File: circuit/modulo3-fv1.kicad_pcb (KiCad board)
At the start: 2 copper layers, 84 x 52 mm, 57 parts, among them J2 HOLE, J4 HOLE, J5 HOLE, J7 HOLE, U1 OPA1642, U10 TLE2426, U2 FV1_CONN, U3 FV-1, U4 PWR_CONN, U5 LM1117 3V3, U6 DIFFAUDIO, U7 AD5142A, U8 AMPCTRL, U9 PREAMP, Y1 32768Hz

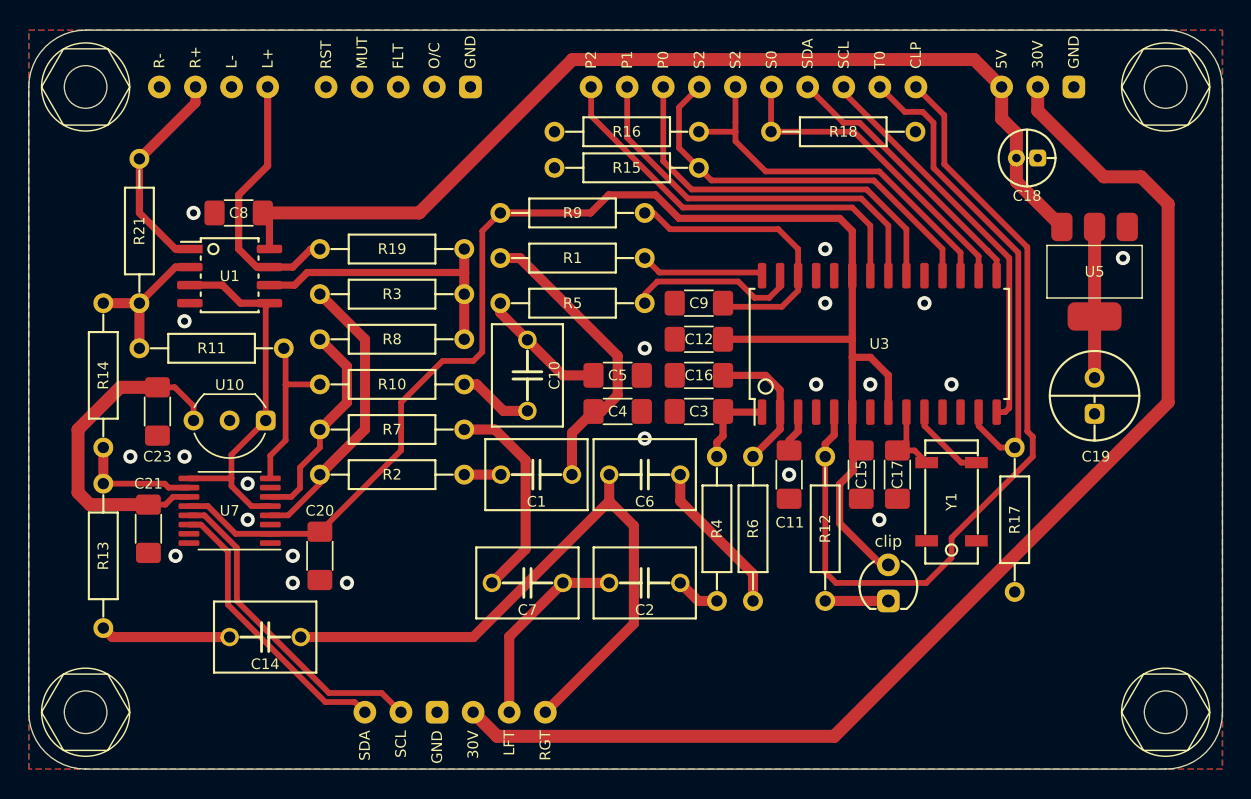
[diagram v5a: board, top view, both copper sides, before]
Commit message: tweaked power amp and fv1
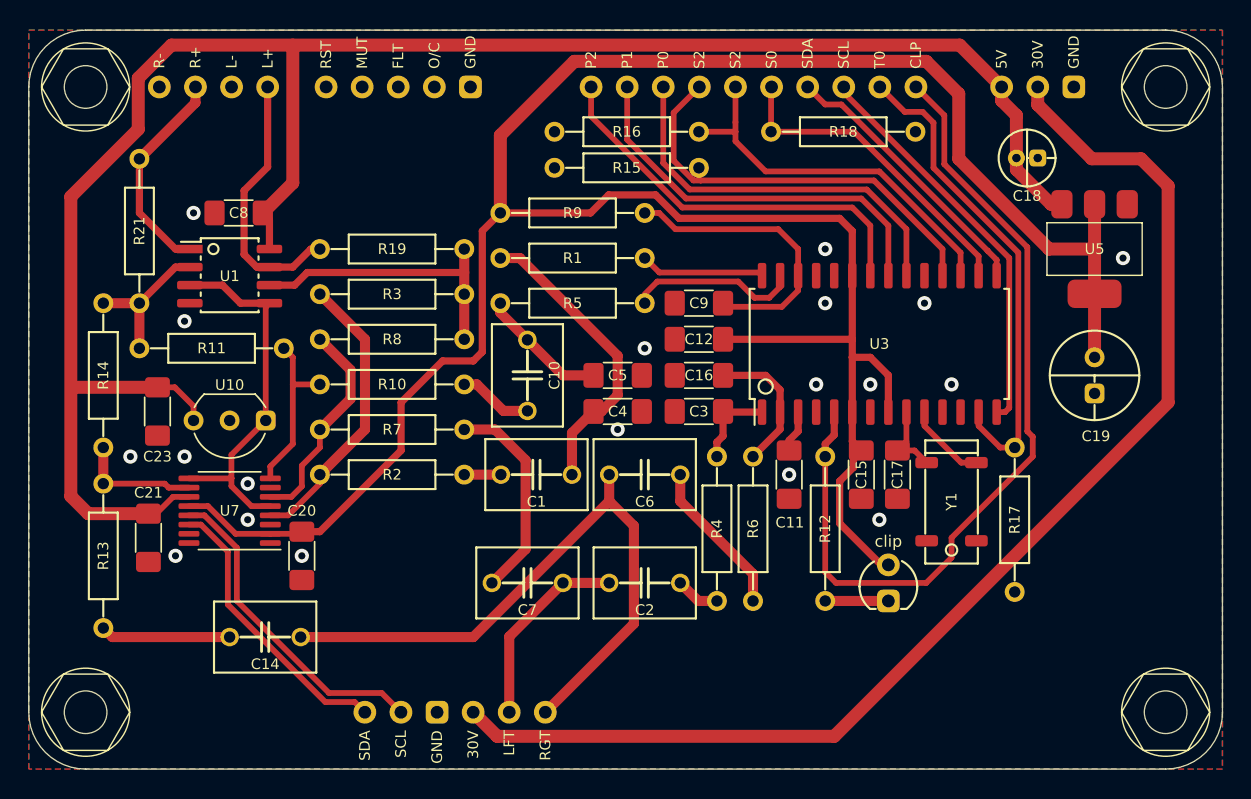
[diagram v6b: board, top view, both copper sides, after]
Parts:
- U4: value PWR_CONN -> POWER
- moved U5 1.59 mm to (125.0, 65.4)
- moved C19 1.44 mm to (125.0, 74.3)
- moved C20 1.27 mm to (69.2, 87.0)
- moved C21 0.63 mm to (58.4, 85.7)
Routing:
- net +3V3: track 116.8 -> 174.6 mm
- net +5V: track 95.3 -> 139.2 mm
- net /S2: track 28.2 -> 30.3 mm
- net GND: vias 21 -> 19

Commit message: ready to panelize
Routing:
- net GND: track 0.00 -> 1.73 mm
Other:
- board text added: "2023/03/19"
- board text added: "modulo3-fv1"
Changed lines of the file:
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@@
   (gr_line (start 50 98) (end 50 54)
     (stroke (width 0.05) (type solid)) (layer "Edge.Cuts"))
+  (gr_text "modulo3-fv1" (at 111.76 95.885) (layer "F.SilkS")
+    (effects (font (size 1.9 1.9) (thickness 0.3)))
+  )
+  (gr_text "2023/03/19" (at 112.03 99.885) (layer "F.SilkS")
+    (effects (font (size 2 2) (thickness 0.3)))
+  )
   (segment (start 88.225 78.35) (end 89.74 76.835) (width 0.7112) (layer "F.Cu") (net 1))
   (segment (start 91.44 72.920797) (end 91.44 75.692) (width 0.7112) (layer "F.Cu") (net 1))
@@
   (segment (start 90.845 88.9) (end 87.59 88.9) (width 0.7112) (layer "F.Cu") (net 4))
   (segment (start 83.81 98) (end 83.81 92.68) (width 0.7112) (layer "F.Cu") (net 4))
+  (segment (start 66.9975 84.795) (end 65.745 84.795) (width 0.4064) (layer "F.Cu") (net 5))
+  (segment (start 65.745 84.795) (end 65.405 84.455) (width 0.4064) (layer "F.Cu") (net 5))
   (via (at 60.96 70.485) (size 1) (drill 0.5) (layers "F.Cu" "B.Cu") (free) (net 5))
   (via (at 106.045 65.405) (size 1) (drill 0.5) (layers "F.Cu" "B.Cu") (free) (net 5))

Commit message: attempt to send to fab: part II
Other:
- board text added: "2023/04/16"
- board text removed: "2023/03/19"
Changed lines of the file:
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@@
     (effects (font (size 1.9 1.9) (thickness 0.3)))
   )
-  (gr_text "2023/03/19" (at 112.03 99.885) (layer "F.SilkS")
+  (gr_text "2023/04/16" (at 112.03 99.885) (layer "F.SilkS")
     (effects (font (size 2 2) (thickness 0.3)))
   )
